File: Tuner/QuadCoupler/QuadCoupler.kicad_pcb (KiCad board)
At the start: 2 copper layers, 100 x 100 mm, 102 parts, among them J1 Conn_01x01, J10 Conn_01x02, J11 Conn_01x01, J12 Conn_01x01, J13 Conn_01x01, J14 Conn_01x01, J15 Conn_01x01, J17 Conn_01x01, J19 Conn_01x02, J2 Conn_Coaxial, J21 Conn_01x01, J22 Conn_01x01, J23 Conn_01x01, J24 Conn_01x01, J3 Conn_Coaxial, J4 Conn_Coaxial, J5 Conn_Coaxial, J6 Conn_Coaxial, J7 Conn_01x01, J8 Conn_01x01, J9 Conn_01x01

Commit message: A few tweaks
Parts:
- added C20: NC, Capacitors_THT:C_Disc_D5.0mm_W2.5mm_P5.00mm, F.Cu at (103.1, 48.4)
- added C21: NC, Capacitors_THT:C_Disc_D5.0mm_W2.5mm_P5.00mm, F.Cu at (51.5, 68.0)
- added C22: NC, Capacitors_THT:C_Disc_D5.0mm_W2.5mm_P5.00mm, F.Cu at (97.1, 131.8)
- added C23: NC, Capacitors_THT:C_Disc_D5.0mm_W2.5mm_P5.00mm, F.Cu at (49.4, 107.5)
- moved J13 7.48 mm to (43.9, 107.1)
- moved J14 7.35 mm to (44.1, 100.1)
- moved J12 4.76 mm to (45.2, 77.3)
- moved J17 4.64 mm to (45.2, 70.7)
- moved JP9 1.34 mm to (94.1, 128.4)
- moved D8 1.27 mm to (88.5, 137.8)
- moved JP6 1.19 mm to (99.8, 49.5)
- moved R20 1.14 mm to (82.7, 137.7)
- moved R19 1.13 mm to (85.8, 130.1)
- moved C4 1.07 mm to (79.7, 130.3)
- moved D6 0.97 mm to (91.1, 137.8)
- moved JP8 0.93 mm to (76.5, 134.0)
- moved D1 0.88 mm to (96.9, 41.8)
- moved R18 0.79 mm to (91.4, 49.5)
- moved R15 0.78 mm to (88.4, 41.8)
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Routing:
- net Net-(C12-Pad1): track 75.5 -> 78.7 mm
- net Net-(C18-Pad1): track 17.2 -> 20.3 mm
- net Net-(C13-Pad2): track 74.8 -> 78.0 mm
- net Net-(C17-Pad1): track 26.4 -> 29.4 mm
- net Net-(C16-Pad1): track 16.5 -> 19.1 mm
- net Net-(D6-Pad2): track 61.7 -> 63.4 mm
- net Net-(C15-Pad1): track 28.6 -> 30.0 mm
- net GND: track 4.17 -> 3.46 mm
- net Net-(C1-Pad1): track 11.3 -> 10.8 mm
- net Net-(D6-Pad1): track 8.57 -> 8.05 mm

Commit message: Actually tuning code now!
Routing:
- net Net-(C12-Pad2): track 63.6 -> 61.7 mm
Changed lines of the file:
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@@
     (thickness 1.6)
     (drawings 58)
-    (tracks 347)
+    (tracks 346)
     (zones 0)
     (modules 106)
@@
   )
   (setup
-    (last_trace_width 0.25)
+    (last_trace_width 2)
     (user_trace_width 0.35)
     (user_trace_width 0.5)
@@
   (segment (start 90.2462 109.6391) (end 90.1954 109.6899) (width 2) (layer B.Cu) (net 23))
   (segment (start 94.2086 109.474) (end 94.0435 109.6391) (width 2) (layer B.Cu) (net 23))
+  (segment (start 94.0435 122.3391) (end 94.0435 123.65862) (width 2) (layer B.Cu) (net 24))
+  (segment (start 94.0435 123.65862) (end 97.14992 126.76504) (width 2) (layer B.Cu) (net 24))
   (segment (start 94.10192 128.35636) (end 95.5586 128.35636) (width 2) (layer B.Cu) (net 24))
   (segment (start 95.5586 128.35636) (end 97.14992 126.76504) (width 2) (layer B.Cu) (net 24))
   (segment (start 97.14992 126.76504) (end 100.05568 126.76504) (width 2) (layer B.Cu) (net 24))
   (segment (start 100.05568 126.76504) (end 100.08108 126.73964) (width 2) (layer B.Cu) (net 24))
-  (segment (start 90.1954 122.3899) (end 90.1954 124.7902) (width 2) (layer B.Cu) (net 24))
-  (segment (start 92.3544 126.8984) (end 94.10192 128.35636) (width 2) (layer B.Cu) (net 24) (status 20))
-  (segment (start 90.1954 124.7902) (end 92.3544 126.8984) (width 2) (layer B.Cu) (net 24))
   (segment (start 94.0435 122.3391) (end 101.9937 122.3391) (width 2) (layer B.Cu) (net 24))
   (segment (start 101.9937 122.3391) (end 102.6668 121.666) (width 2) (layer B.Cu) (net 24))

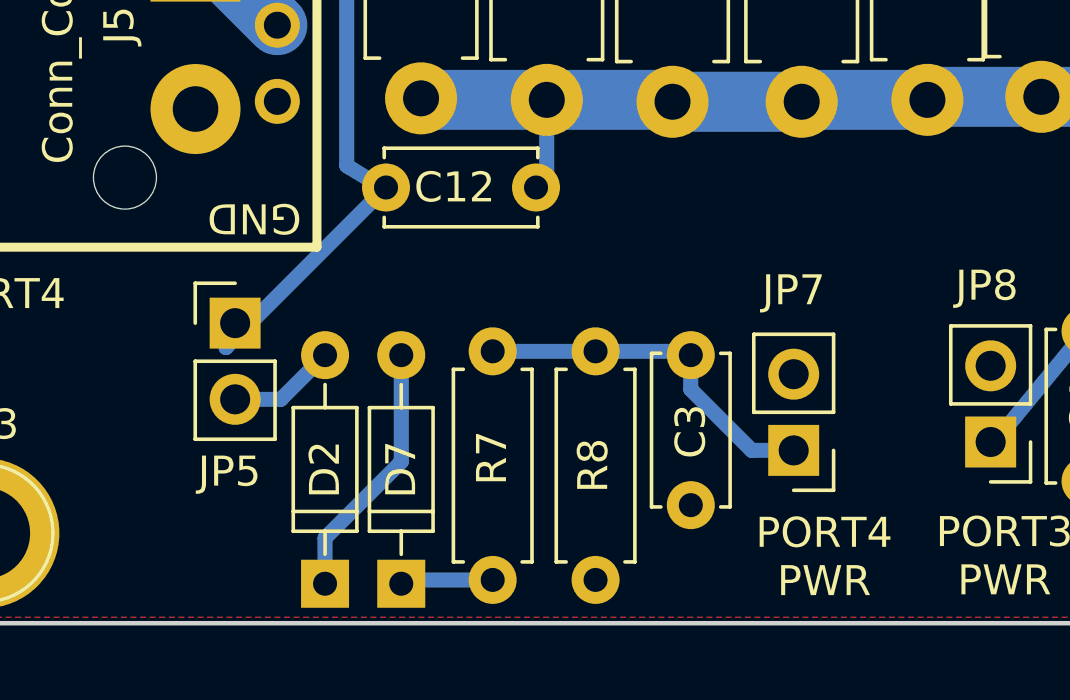
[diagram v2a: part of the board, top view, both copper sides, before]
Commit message: Changed bypass method on delay lines
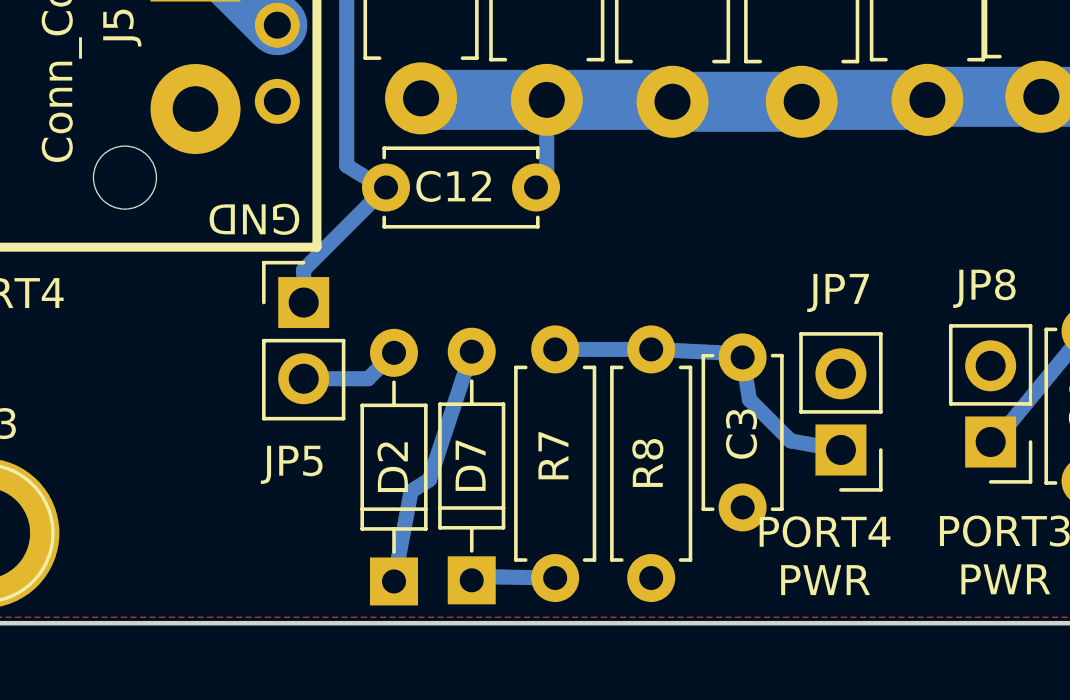
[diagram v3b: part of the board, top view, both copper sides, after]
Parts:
- moved JP5 2.39 mm to (53.6, 129.3)
- moved D7 2.35 mm to (59.2, 138.6)
- moved D2 2.30 mm to (56.7, 138.6)
- moved R7 2.08 mm to (62.0, 130.9)
- moved R8 1.86 mm to (65.2, 138.5)
- moved C3 1.73 mm to (68.3, 131.1)
- moved JP7 1.57 mm to (71.6, 134.2)
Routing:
- net Net-(C12-Pad1): track 78.7 -> 75.4 mm
- net Net-(C3-Pad1): track 12.1 -> 11.4 mm
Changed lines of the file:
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@@
     (thickness 1.6)
     (drawings 58)
-    (tracks 346)
+    (tracks 348)
     (zones 0)
     (modules 106)
@@
   )
   (setup
-    (last_trace_width 2)
+    (last_trace_width 0.5)
     (user_trace_width 0.35)
     (user_trace_width 0.5)
@@
   )
   (module Capacitors_THT:C_Disc_D5.0mm_W2.5mm_P5.00mm (layer F.Cu)
-    (at 66.548 131.064 270)
+    (at 68.2752 131.1402 270)
     (descr "C, Disc series, Radial, pin pitch=5.00mm, , diameter*width=5*2.5mm^2, Capacitor, http://cdn-reichelt.de/documents/datenblatt/B300/DS_KERKO_TC.pdf")
     (tags "C Disc series Radial pin pitch 5.00mm  diameter 5mm width 2.5mm Capacitor")
@@
   )
   (module Resistors_THT:R_Axial_DIN0207_L6.3mm_D2.5mm_P7.62mm_Horizontal (layer F.Cu)
-    (at 59.944 130.937 270)
+    (at 62.0268 130.8735 270)
     (descr "Resistor, Axial_DIN0207 series, Axial, Horizontal, pin pitch=7.62mm, 0.25W = 1/4W, length*diameter=6.3*2.5mm^2, http://cdn-reichelt.de/documents/datenblatt/B400/1_4W%23YAG.pdf")
     (tags "Resistor Axial_DIN0207 series Axial Horizontal pin pitch 7.62mm 0.25W = 1/4W length 6.3mm diameter 2.5mm")
@@
   )
   (module Resistors_THT:R_Axial_DIN0207_L6.3mm_D2.5mm_P7.62mm_Horizontal (layer F.Cu)
-    (at 63.373 138.557 90)
+    (at 65.2272 138.4935 90)
     (descr "Resistor, Axial_DIN0207 series, Axial, Horizontal, pin pitch=7.62mm, 0.25W = 1/4W, length*diameter=6.3*2.5mm^2, http://cdn-reichelt.de/documents/datenblatt/B400/1_4W%23YAG.pdf")
     (tags "Resistor Axial_DIN0207 series Axial Horizontal pin pitch 7.62mm 0.25W = 1/4W length 6.3mm diameter 2.5mm")
@@
   )
   (module Diodes_THT:D_DO-35_SOD27_P7.62mm_Horizontal (layer F.Cu)
-    (at 54.356 138.684 90)
+    (at 56.6547 138.6078 90)
     (descr "D, DO-35_SOD27 series, Axial, Horizontal, pin pitch=7.62mm, , length*diameter=4*2mm^2, , http://www.diodes.com/_files/packages/DO-35.pdf")
     (tags "D DO-35_SOD27 series Axial Horizontal pin pitch 7.62mm  length 4mm diameter 2mm")
@@
   )
   (module Diodes_THT:D_DO-35_SOD27_P7.62mm_Horizontal (layer F.Cu)
-    (at 56.896 138.684 90)
+    (at 59.2455 138.5697 90)
     (descr "D, DO-35_SOD27 series, Axial, Horizontal, pin pitch=7.62mm, , length*diameter=4*2mm^2, , http://www.diodes.com/_files/packages/DO-35.pdf")
     (tags "D DO-35_SOD27 series Axial Horizontal pin pitch 7.62mm  length 4mm diameter 2mm")
@@
   )
   (module Pin_Headers:Pin_Header_Straight_1x02_Pitch2.54mm (layer F.Cu)
-    (at 51.3588 129.9972)
+    (at 53.6448 129.3114)
     (descr "Through hole straight pin header, 1x02, 2.54mm pitch, single row")
     (tags "Through hole pin header THT 1x02 2.54mm single row")
-    (fp_text reference JP5 (at -0.18796 4.953) (layer F.SilkS)
+    (fp_text reference JP5 (at -0.3048 5.3086) (layer F.SilkS)
       (effects (font (size 1 1) (thickness 0.15)))
     )
@@
   )
   (module Pin_Headers:Pin_Header_Straight_1x02_Pitch2.54mm (layer F.Cu)
-    (at 69.977 134.239 180)
+    (at 71.5518 134.2263 180)
     (descr "Through hole straight pin header, 1x02, 2.54mm pitch, single row")
     (tags "Through hole pin header THT 1x02 2.54mm single row")
@@
   (segment (start 69.088 50.1015) (end 69.215 49.9745) (width 0.5) (layer B.Cu) (net 3) (status 30))
   (segment (start 66.04 49.9745) (end 69.215 49.9745) (width 0.5) (layer B.Cu) (net 3) (status 20))
-  (segment (start 66.548 131.064) (end 66.548 132.207) (width 0.5) (layer B.Cu) (net 4))
-  (segment (start 68.58 134.239) (end 69.977 134.239) (width 0.5) (layer B.Cu) (net 4))
-  (segment (start 66.548 132.207) (end 68.58 134.239) (width 0.5) (layer B.Cu) (net 4))
-  (segment (start 63.373 130.937) (end 66.421 130.937) (width 0.5) (layer B.Cu) (net 4))
-  (segment (start 66.421 130.937) (end 66.548 131.064) (width 0.5) (layer B.Cu) (net 4))
-  (segment (start 59.944 130.937) (end 63.373 130.937) (width 0.5) (layer B.Cu) (net 4))
+  (segment (start 68.2752 131.1402) (end 68.5038 132.5499) (width 0.5) (layer B.Cu) (net 4) (status 10))
+  (segment (start 69.8754 133.9215) (end 71.5518 134.2263) (width 0.5) (layer B.Cu) (net 4) (status 20))
+  (segment (start 68.5038 132.5499) (end 69.8754 133.9215) (width 0.5) (layer B.Cu) (net 4))
+  (segment (start 65.2272 130.8735) (end 68.1482 131.0132) (width 0.5) (layer B.Cu) (net 4) (status 10))
+  (segment (start 68.1482 131.0132) (end 68.2752 131.1402) (width 0.5) (layer B.Cu) (net 4) (status 30))
+  (segment (start 62.0268 130.8735) (end 65.2272 130.8735) (width 0.5) (layer B.Cu) (net 4) (status 10))
   (segment (start 76.5429 133.9596) (end 76.6699 133.9596) (width 0.5) (layer B.Cu) (net 5) (status 30))
   (segment (start 76.6699 133.9596) (end 79.7052 130.26644) (width 0.5) (layer B.Cu) (net 5) (status 20))
@@
   (segment (start 102.68966 40.92194) (end 106.15676 40.99814) (width 0.5) (layer B.Cu) (net 6))
   (segment (start 116.69014 40.99814) (end 106.15676 40.99814) (width 0.5) (layer B.Cu) (net 6))
-  (segment (start 51.3588 132.5372) (end 52.8828 132.5372) (width 0.5) (layer B.Cu) (net 7))
-  (segment (start 52.8828 132.5372) (end 54.356 131.064) (width 0.5) (layer B.Cu) (net 7))
+  (segment (start 53.6448 131.8514) (end 55.7911 131.8514) (width 0.5) (layer B.Cu) (net 7) (status 400000))
+  (segment (start 55.7911 131.8514) (end 56.6547 130.9878) (width 0.5) (layer B.Cu) (net 7) (status 800000))
+  (segment (start 56.6547 130.9878) (end 56.6547 130.7084) (width 0.5) (layer B.Cu) (net 7) (status 30))
   (segment (start 57.277 47.2948) (end 59.9948 47.2948) (width 0.5) (layer B.Cu) (net 8))
   (segment (start 60.2615 48.4505) (end 60.6425 49.8475) (width 0.5) (layer B.Cu) (net 8) (status 20))
@@
   (segment (start 60.6425 42.9895) (end 61.595 45.212) (width 0.5) (layer B.Cu) (net 13) (status 10))
   (segment (start 61.595 45.212) (end 63.246 49.9745) (width 0.5) (layer B.Cu) (net 13) (status 20))
-  (segment (start 54.356 138.684) (end 54.356 137.16) (width 0.5) (layer B.Cu) (net 14))
-  (segment (start 56.896 134.62) (end 56.896 131.064) (width 0.5) (layer B.Cu) (net 14))
-  (segment (start 54.356 137.16) (end 56.896 134.62) (width 0.5) (layer B.Cu) (net 14))
+  (segment (start 56.6547 138.6078) (end 57.2262 135.5979) (width 0.5) (layer B.Cu) (net 14) (status 10))
+  (segment (start 57.8358 135.2169) (end 59.2455 130.9497) (width 0.5) (layer B.Cu) (net 14) (status 20))
+  (segment (start 57.2262 135.5979) (end 57.8358 135.2169) (width 0.5) (layer B.Cu) (net 14))
   (segment (start 88.5444 130.1496) (end 89.34704 132.2832) (width 0.5) (layer B.Cu) (net 15) (status 10))
   (segment (start 89.95664 134.0358) (end 91.1352 137.7696) (width 0.5) (layer B.Cu) (net 15) (status 20))
   (segment (start 89.34704 132.2832) (end 89.95664 134.0358) (width 0.5) (layer B.Cu) (net 15))
-  (segment (start 59.944 138.557) (end 57.023 138.557) (width 0.5) (layer B.Cu) (net 16))
-  (segment (start 57.023 138.557) (end 56.896 138.684) (width 0.5) (layer B.Cu) (net 16))
+  (segment (start 62.0268 138.4935) (end 59.3725 138.4427) (width 0.5) (layer B.Cu) (net 16) (status 20))
+  (segment (start 59.3725 138.4427) (end 59.2455 138.5697) (width 0.5) (layer B.Cu) (net 16) (status 30))
   (segment (start 88.5444 137.7696) (end 85.86724 137.5918) (width 0.5) (layer B.Cu) (net 17) (status 10))
   (segment (start 85.86724 137.5918) (end 85.76564 137.6934) (width 0.5) (layer B.Cu) (net 17) (status 30))
@@
   (segment (start 107.0102 63.9064) (end 108.6866 62.23) (width 2) (layer B.Cu) (net 22))
   (segment (start 104.394 63.9064) (end 104.7496 63.9064) (width 2) (layer B.Cu) (net 22))
+  (segment (start 53.6448 129.3114) (end 53.6448 128.2192) (width 0.5) (layer B.Cu) (net 23) (status 400000))
+  (segment (start 53.6448 128.2192) (end 56.388 125.476) (width 0.5) (layer B.Cu) (net 23) (status 800000))
+  (segment (start 56.388 125.476) (end 56.388 125.5776) (width 0.5) (layer B.Cu) (net 23))
   (segment (start 54.3649 107.4547) (end 54.3649 110.2741) (width 2) (layer B.Cu) (net 23))
   (segment (start 54.3649 110.2741) (end 54.0855 110.5535) (width 2) (layer B.Cu) (net 23))
@@
   (segment (start 102.2477 109.6391) (end 102.4128 109.474) (width 2) (layer B.Cu) (net 23))
   (segment (start 86.106 109.5121) (end 86.2838 109.6899) (width 1) (layer B.Cu) (net 23))
-  (segment (start 51.3588 129.9972) (end 51.054 130.81) (width 0.5) (layer B.Cu) (net 23) (status 10))
-  (segment (start 51.054 130.81) (end 56.388 125.476) (width 0.5) (layer B.Cu) (net 23))
   (segment (start 57.5564 109.8042) (end 61.6966 109.8042) (width 2) (layer B.Cu) (net 23))
   (segment (start 61.6966 109.8042) (end 61.7474 109.855) (width 2) (layer B.Cu) (net 23))

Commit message: JLCPCB order 2019-03-25
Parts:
- added C24: NC, Capacitors_THT:C_Disc_D5.0mm_W2.5mm_P5.00mm, F.Cu at (59.7, 85.5)
- added C25: NC, Capacitors_THT:C_Disc_D5.0mm_W2.5mm_P5.00mm, F.Cu at (59.7, 88.6)
- added J16: Conn_01x01, Connectors:1pin, F.Cu at (58.3, 77.3)
- moved C7 15.4 mm to (58.9, 97.7), turned to 270 degrees
- moved J4 1.15 mm to (40.0, 58.7)
- moved J3 0.93 mm to (39.9, 88.9)
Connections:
- C7 pad 1: Net-(C7-Pad1) -> Net-(C24-Pad1)
- J3 pad 1: Net-(C7-Pad1) -> Net-(C24-Pad2)
- TR1 pad 2: Net-(C7-Pad1) -> Net-(C24-Pad1)
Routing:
- net Net-(C7-Pad1): track 22.3 -> 0.00 mm
- net Net-(C24-Pad2): track 0.00 -> 19.3 mm
- net Net-(C24-Pad1): track 0.00 -> 17.6 mm
- net Net-(C15-Pad1): track 30.0 -> 31.5 mm
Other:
- board text added: "HIGHZ"
- board text added: "LOWZ"
- board text removed: "4:1"
- board text removed: "9:1"

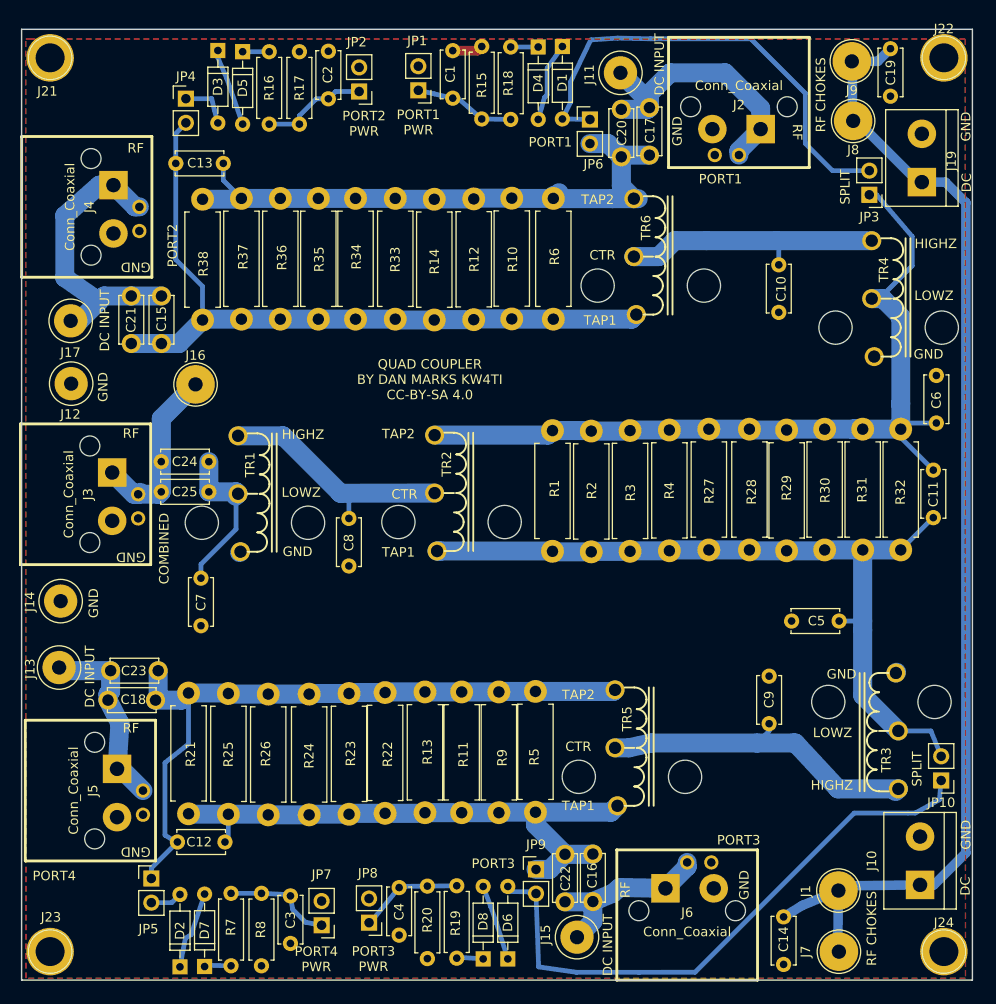
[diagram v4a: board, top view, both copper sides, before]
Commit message: Change named to DirectionalCoupler, fixed order of two pins in QuadCoupler
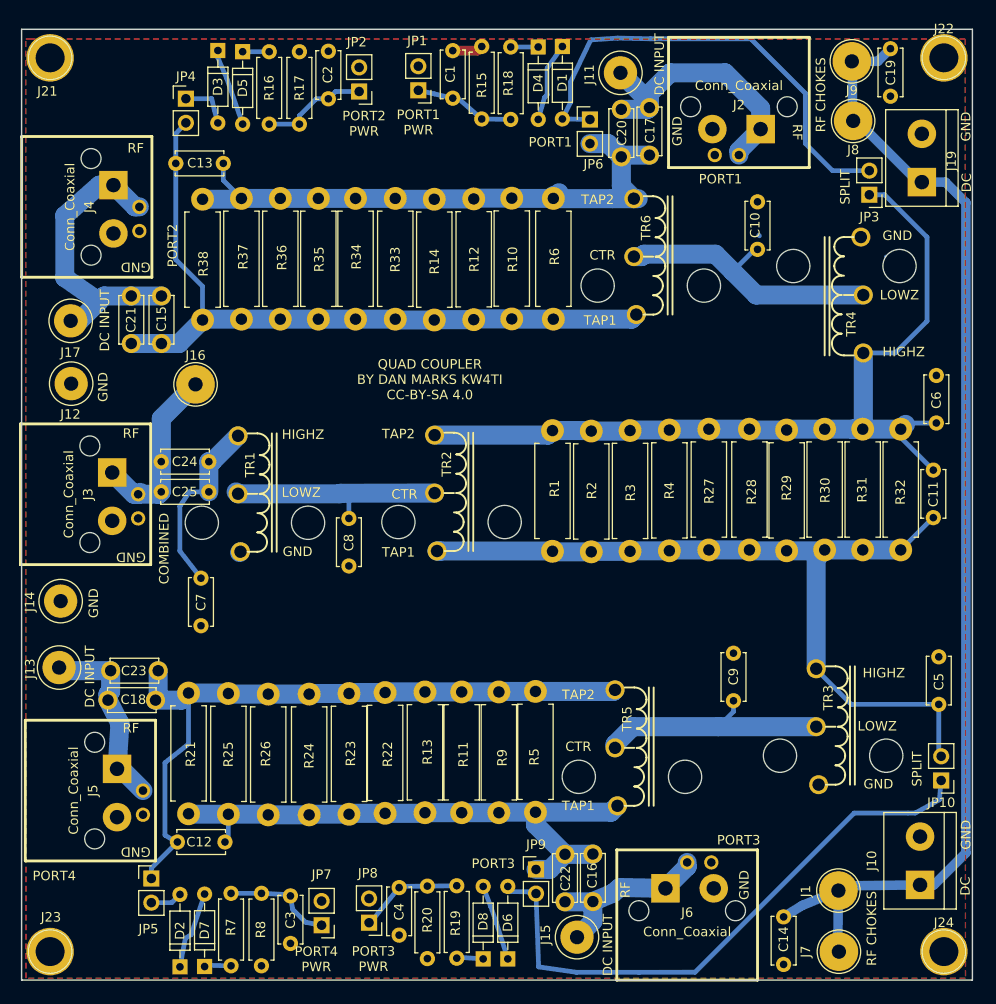
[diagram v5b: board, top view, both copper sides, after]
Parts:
- moved C5 13.7 mm to (136.5, 111.0), turned to 90 degrees
- moved TR3 8.65 mm to (123.6, 113.3), turned to 0 degrees
- moved C9 4.46 mm to (114.9, 110.6)
- moved C10 2.76 mm to (117.4, 63.1), turned to 90 degrees
- moved TR4 0.97 mm to (128.5, 67.9), turned to 180 degrees
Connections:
- TR1 pad 2: Net-(C24-Pad1) -> Net-(C8-Pad1)
- TR1 pad 3: Net-(C8-Pad1) -> Net-(C24-Pad1)
- TR3 pad 2: Net-(C11-Pad2) -> Net-(C9-Pad1)
- TR3 pad 3: Net-(C9-Pad1) -> Net-(C11-Pad2)
- TR4 pad 2: Net-(C11-Pad1) -> Net-(C10-Pad1)
- TR4 pad 3: Net-(C10-Pad1) -> Net-(C11-Pad1)
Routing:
- net Net-(C9-Pad1): track 34.9 -> 25.7 mm
- net Net-(C11-Pad2): track 84.6 -> 87.3 mm
- net Net-(C11-Pad1): track 93.9 -> 96.1 mm
- net (no net): track 0.00 -> 2.12 mm
- net Net-(C24-Pad1): track 17.6 -> 19.6 mm
- net Net-(C8-Pad1): track 26.2 -> 24.3 mm
